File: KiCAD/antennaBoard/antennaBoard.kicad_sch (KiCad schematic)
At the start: 0 parts

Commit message: Add coax
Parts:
- added ANT1: 2.305GHz Patch, Inspirefly:CircularPatchAntenna, symbol Device:Antenna
- added J1: Conn_Coaxial, Connector_Coaxial:MMCX_Molex_73415-0961_Horizontal_0.8mm-PCB, symbol Connector:Conn_Coaxial
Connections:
- new net: ANT1.1 (A), J1.1 (In)
- new net GND: J1.2 (Ext)
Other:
- company: (none) -> Inspirefly
- title: (none) -> 2.305GHz Patch Antenna

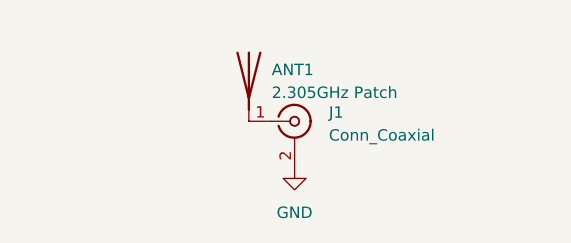
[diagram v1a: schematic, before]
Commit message: Impl 2 coax feed
Use external power divider: APS-02-WBM-LP-DF-CC
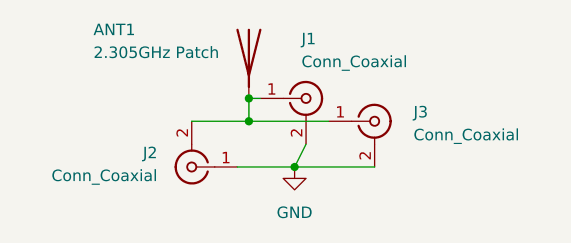
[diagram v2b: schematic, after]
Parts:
- added J2: Conn_Coaxial, Connector_Coaxial:SMA_Amphenol_132289_EdgeMount, symbol Connector:Conn_Coaxial
- added J3: Conn_Coaxial, Inspirefly:CONN_732511350_MOL, symbol Connector:Conn_Coaxial
- J1: footprint Connector_Coaxial:MMCX_Molex_73415-0961_Horizontal_0.8mm-PCB -> Inspirefly:CONN_732511350_MOL
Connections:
- net GND: now also J2.1 (In), J3.2 (Ext)
- net at ANT1.1 (A), J1.1 (In): now also J2.2 (Ext), J3.1 (In)
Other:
- moved on the sheet: ANT1, J1
